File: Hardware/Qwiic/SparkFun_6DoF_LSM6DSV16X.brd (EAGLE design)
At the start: 25.4 x 25.4 mm, 70 parts, among them J1 QWIIC_RIGHT_ANGLE, J2 QWIIC_RIGHT_ANGLE, U2 LSM6DSV16X

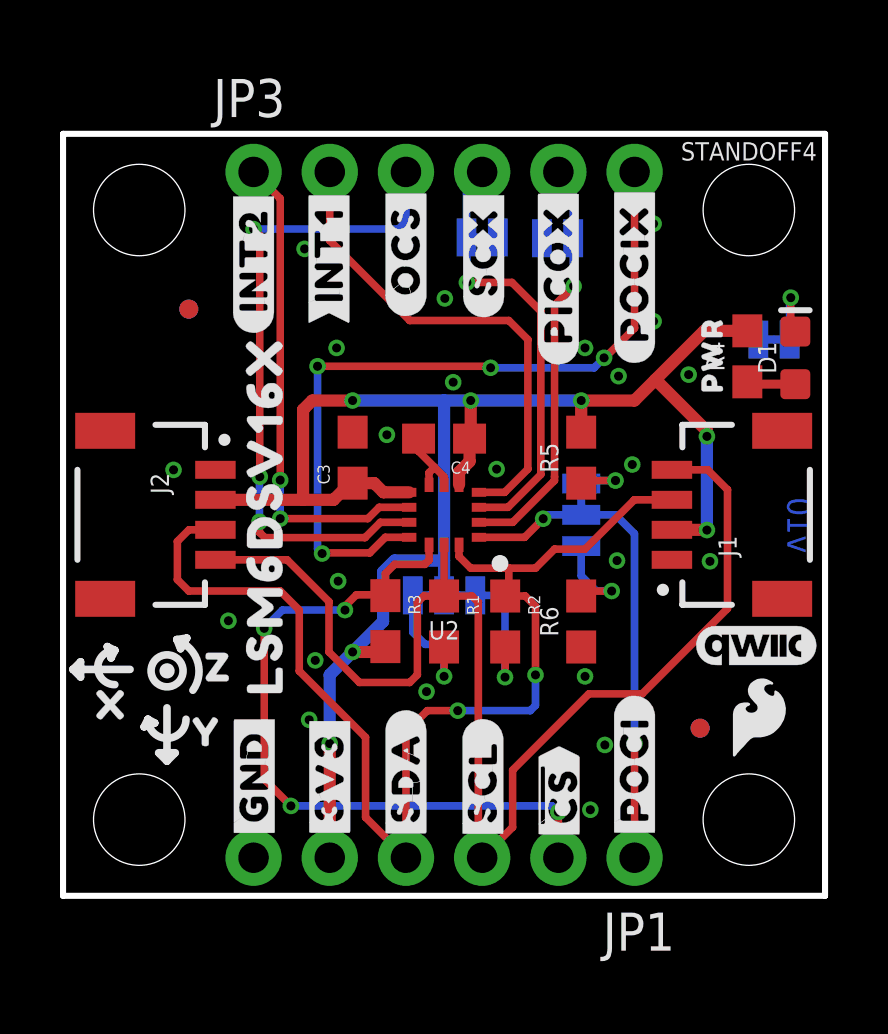
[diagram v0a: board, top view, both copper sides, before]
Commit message: Changes design to design with filter
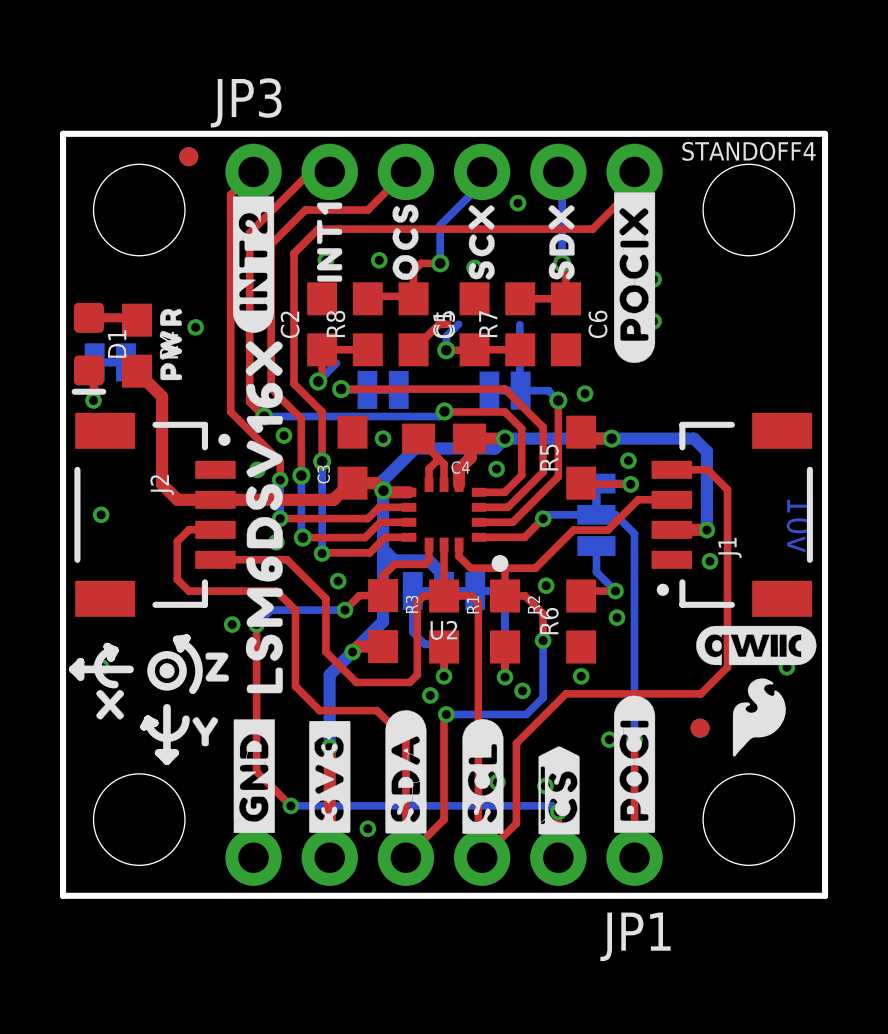
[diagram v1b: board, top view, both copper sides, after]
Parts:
- removed FRAME1: FRAME-LETTER, SparkFun-Aesthetics:CREATIVE_COMMONS
- removed U$19: (no value), bot:#INT1#9
- removed U$20: (no value), bot:#OCS#7
- removed U$21: (no value), top:LSM6DSV16X37
- added C1, C2, C5, C6: 110pF, SparkFun-Capacitors:0603
- added FRAME2: FRAME-LEDGER, SparkFun-Aesthetics:CREATIVE_COMMONS
- added R7, R8: 0, SparkFun-Resistors:0603
- added U$32: (no value), top:OCS17
- added U$41: (no value), top:INT16
- added U$42: (no value), top:#SDX#20
- added U$43: (no value), top:#SCX#19
- added U$44: (no value), top:#FILT1#21
- added U$45: (no value), top:#FILT2#21
- added U$46: (no value), top:LSM6DSV16X37
- U$10: device top:#SCX#9 -> top:SCX18
- U$11: device ISMTop:#PICOX#10 -> top:SDX19
- U$23: device bot:#SCX#8 -> top:SCX18
- U$30: device bot:#SDX#28 -> top:SDX19
- U$7: device top:#INT1#9 -> top:INT16
- U$9: device top:#OCS#8 -> top:OCS17
- moved D1 23.6 mm to (0.86, 18.4), turned to 270 degrees
- moved LED 22.1 mm to (1.57, 17.8), turned to 0 degrees
- moved U$16 22.1 mm to (1.65, 19.3)
- moved R4 20.3 mm to (2.46, 18.3), turned to 270 degrees
- moved U$28 18.0 mm to (3.61, 18.4)
- moved SCX 6.06 mm to (10.7, 16.9)
- moved SDX 5.37 mm to (14.7, 16.8)
- moved FD1 5.08 mm to (4.19, 24.6)
- moved FID1 5.08 mm to (4.19, 24.6)
- moved U$30 2.54 mm to (16.5, 21.6)
- moved U$23 2.52 mm to (13.8, 21.6)
- moved U$31 2.29 mm to (7.98, 12.7)
- moved U$11 1.12 mm to (16.6, 21.8)
- moved U$14 0.63 mm to (15.2, 13.3)
- moved U$13 0.57 mm to (15.1, 12.1)
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- renumbered U$12 to U$47
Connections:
- removed net SCX: JP3.4, SCX.2, U2.P3
- removed net SDX/PICO_AUX: JP3.5, SDX.2, U2.P2
- new net SCX/AH2/QVAR2: C5.1, JP3.4, R8.2
- new net SCX/AH2/QVAR2_FILTER: C2.1, R8.1, SCX.2, U2.P3
- new net SDX/AH1/QVAR1: C6.1, JP3.5, R7.2
- new net SDX/AH1/QVAR1_FILTER: C1.1, R7.1, SDX.2, U2.P2
- net GND: now also C1.2, C2.2, C5.2, C6.2
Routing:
- net SCX/AH2/QVAR2_FILTER: track 0.00 -> 15.8 mm, vias 0 -> 2
- net SCX: track 14.7 -> 0.00 mm, vias 1 -> 0
- net SDX/PICO_AUX: track 13.9 -> 0.00 mm, vias 1 -> 0
- net SDX/AH1/QVAR1_FILTER: track 0.00 -> 12.9 mm, vias 0 -> 2
- net SCX/AH2/QVAR2: track 0.00 -> 7.78 mm, vias 0 -> 1
- net SDX/AH1/QVAR1: track 0.00 -> 5.86 mm, vias 0 -> 1
- net 3.3V: track 56.8 -> 50.9 mm, vias 7 -> 6
- net INT1: track 16.5 -> 22.0 mm, vias 0 -> 2
- net OCS: track 22.3 -> 19.5 mm, vias 3 -> 2
- net GND: track 2.56 -> 4.38 mm, vias 23 -> 29
- net SCL: track 43.3 -> 44.9 mm
- net SDA/PICO: track 39.9 -> 40.6 mm
- net INT2: track 16.4 -> 17.0 mm
- net POCI_AUX: track 25.8 -> 26.3 mm, vias 4 -> 2
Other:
- board text added: "Elias Santistevan"
- board text added: "v01"
- board text removed: "v10"

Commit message: Adds labels, fixes various DRC issues
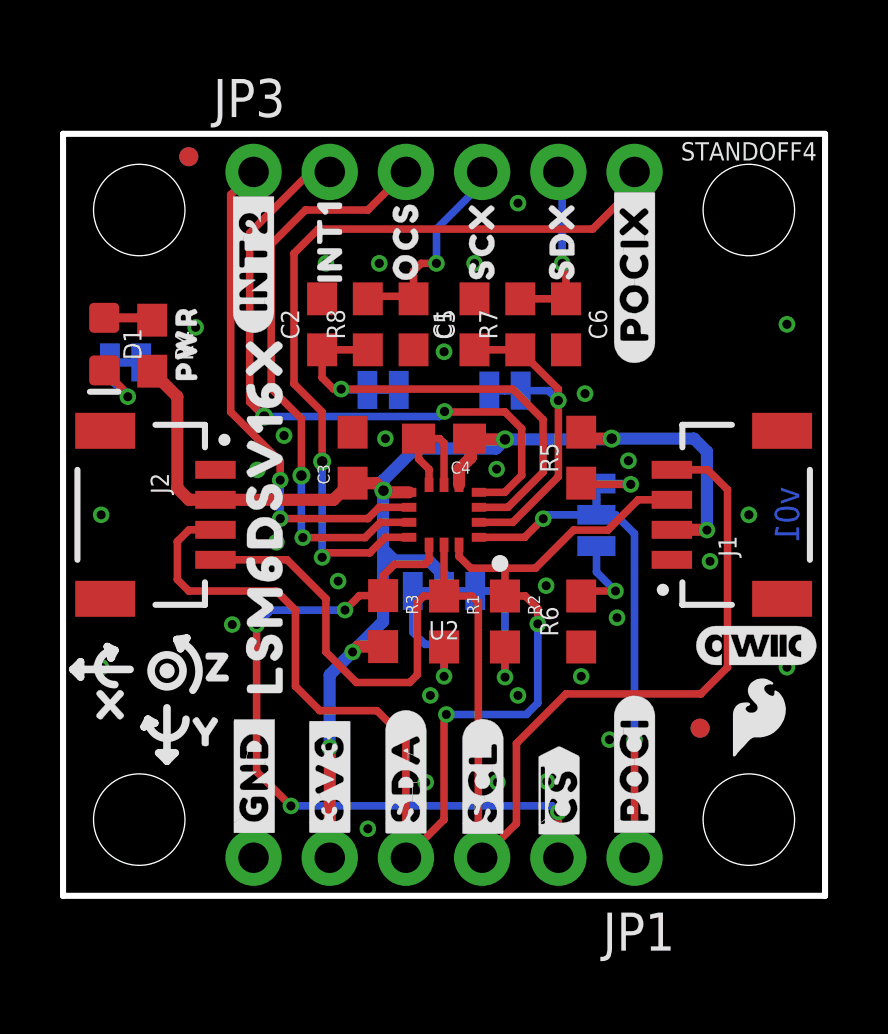
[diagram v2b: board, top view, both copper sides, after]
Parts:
- removed U$23: (no value), top:SCX18
- removed U$30: (no value), top:SDX19
- removed U$32: (no value), top:OCS17
- removed U$41: (no value), top:INT16
- removed U$44: (no value), top:#FILT1#21
- removed U$45: (no value), top:#FILT2#21
- added U$12: (no value), bot:#AH1#32
- added U$19: (no value), bot:#AH2#32
- added U$20: (no value), bot:#OCS#32
- added U$21: (no value), top:#INT1#25
- moved LED 0.51 mm to (2.08, 17.8)
- moved R4 0.51 mm to (2.97, 18.3)
- moved U$28 0.51 mm to (4.11, 18.4)
- moved D1 0.51 mm to (1.37, 18.4)
- moved U$16 0.51 mm to (2.16, 19.3)
- moved LOGO3 0.28 mm to (4.37, 12.7)
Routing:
- net SDX/AH1/QVAR1_FILTER: track 12.9 -> 11.0 mm, vias 2 -> 1
- net 3.3V: track 50.9 -> 50.0 mm
- net SCX/AH2/QVAR2: track 7.78 -> 7.23 mm
- net GND: track 4.38 -> 3.99 mm, vias 29 -> 31
- net SCX/AH2/QVAR2_FILTER: track 15.8 -> 15.7 mm, vias 2 -> 1

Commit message: Updates measures, fixes various DRC issues in micro
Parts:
- moved FRAME2 10.2 mm to (-17.8, -22.9)
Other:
- board text added: "Units in Inches"
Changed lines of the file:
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@@
 <layer number="45" name="Holes" color="7" fill="1" visible="yes" active="yes"/>
 <layer number="46" name="Milling" color="3" fill="1" visible="no" active="yes"/>
-<layer number="47" name="Measures" color="7" fill="1" visible="no" active="yes"/>
+<layer number="47" name="Measures" color="7" fill="1" visible="yes" active="yes"/>
 <layer number="48" name="Document" color="7" fill="1" visible="no" active="yes"/>
 <layer number="49" name="Reference" color="13" fill="1" visible="yes" active="yes"/>
@@
 <wire x1="22.5663125" y1="9.3805375" x2="23.2806875" y2="8.6661625" width="0.2032" layer="22"/>
 <wire x1="23.241" y1="9.3805375" x2="22.526625" y2="8.6661625" width="0.2032" layer="22"/>
-<dimension x1="0" y1="25.4" x2="0" y2="0" x3="-8.636" y3="12.7" textsize="1.778" textratio="15" layer="47" unit="inch" visible="yes"/>
-<dimension x1="25.4" y1="25.4" x2="0" y2="25.4" x3="12.7" y3="30.48" textsize="1.778" textratio="15" layer="47" unit="inch" visible="yes"/>
-<dimension x1="5.08" y1="12.7" x2="5.08" y2="0" x3="-5.588" y3="6.35" textsize="1.778" textratio="15" layer="47" unit="inch" visible="yes"/>
+<dimension x1="0" y1="25.4" x2="0" y2="0" x3="-8.636" y3="12.7" textsize="1.778" textratio="15" layer="47" unit="inch"/>
+<dimension x1="25.4" y1="25.4" x2="0" y2="25.4" x3="12.7" y3="30.48" textsize="1.778" textratio="15" layer="47" unit="inch"/>
+<dimension x1="5.08" y1="12.7" x2="5.08" y2="0" x3="-5.588" y3="6.35" textsize="1.778" textratio="15" layer="47" unit="inch"/>
 <dimension x1="2.54" y1="2.54" x2="2.54" y2="0" x3="-1.778" y3="1.27" textsize="1.778" textratio="15" layer="47" unit="inch"/>
-<dimension x1="2.54" y1="22.86" x2="2.54" y2="25.4" x3="-2.54" y3="24.13" textsize="1.778" textratio="15" layer="47" unit="inch" visible="yes"/>
-<dimension x1="2.54" y1="22.86" x2="22.86" y2="22.86" x3="12.7" y3="27.178" textsize="1.778" textratio="15" layer="47" unit="inch" visible="yes"/>
+<dimension x1="2.54" y1="22.86" x2="2.54" y2="25.4" x3="-2.54" y3="24.13" textsize="1.778" textratio="15" layer="47" unit="inch"/>
+<dimension x1="2.54" y1="22.86" x2="22.86" y2="22.86" x3="12.7" y3="27.178" textsize="1.778" textratio="15" layer="47" unit="inch"/>
 <rectangle x1="12.446" y1="13.462" x2="12.4968" y2="13.7668" layer="41"/>
-<text x="12.7" y="-12.7" size="1.778" layer="51" font="vector">Elias Santistevan</text>
+<text x="12.7" y="-22.86" size="1.778" layer="51" font="vector">Elias Santistevan</text>
+<text x="-26.67" y="-3.81" size="1.778" layer="47" font="vector">Units in Inches</text>
+<dimension x1="6.35" y1="1.27" x2="0" y2="1.27" x3="3.175" y3="-7.62" textsize="1.778" layer="47" unit="inch"/>
+<dimension x1="0" y1="0" x2="19.05" y2="0" x3="9.525" y3="-12.7" textsize="1.778" layer="47" unit="inch"/>
 </plain>
 <attributes>
@@
 <attribute name="VALUE" value="0" x="10.922" y="19.05" size="0.6096" layer="27" font="vector" ratio="20" rot="R90" align="top-center"/>
 </element>
-<element name="FRAME2" library="SparkFun-Aesthetics" package="CREATIVE_COMMONS" value="FRAME-LEDGER" x="-17.78" y="-12.7" smashed="yes">
-<attribute name="DESIGNER" value="" x="-17.78" y="-12.7" size="1.778" layer="27" display="off"/>
-<attribute name="REV" value="" x="-17.78" y="-12.7" size="1.778" layer="27" display="off"/>
+<element name="FRAME2" library="SparkFun-Aesthetics" package="CREATIVE_COMMONS" value="FRAME-LEDGER" x="-17.78" y="-22.86" smashed="yes">
+<attribute name="DESIGNER" value="" x="-17.78" y="-22.86" size="1.778" layer="27" display="off"/>
+<attribute name="REV" value="" x="-17.78" y="-22.86" size="1.778" layer="27" display="off"/>
 </element>
 <element name="U$7" library="top" package="INT16" value="" x="8.89" y="21.844" smashed="yes" rot="R90"/>

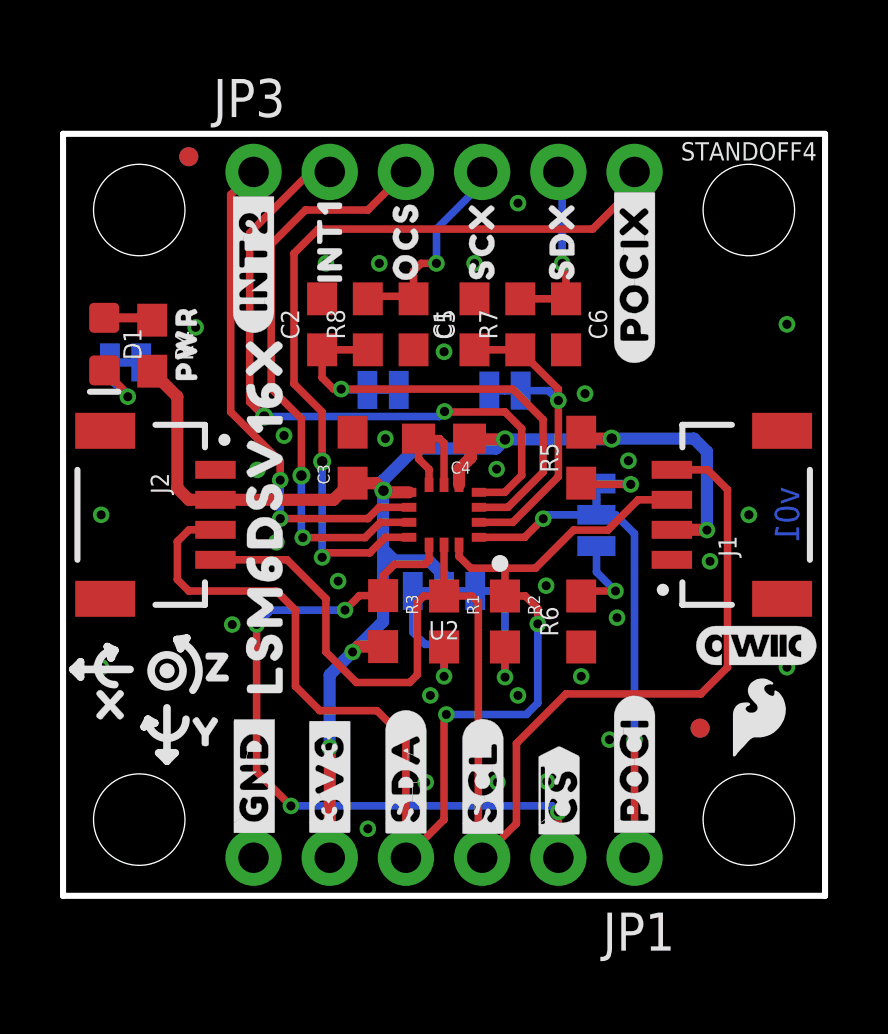
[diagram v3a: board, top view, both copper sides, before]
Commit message: Updates part with silk outline
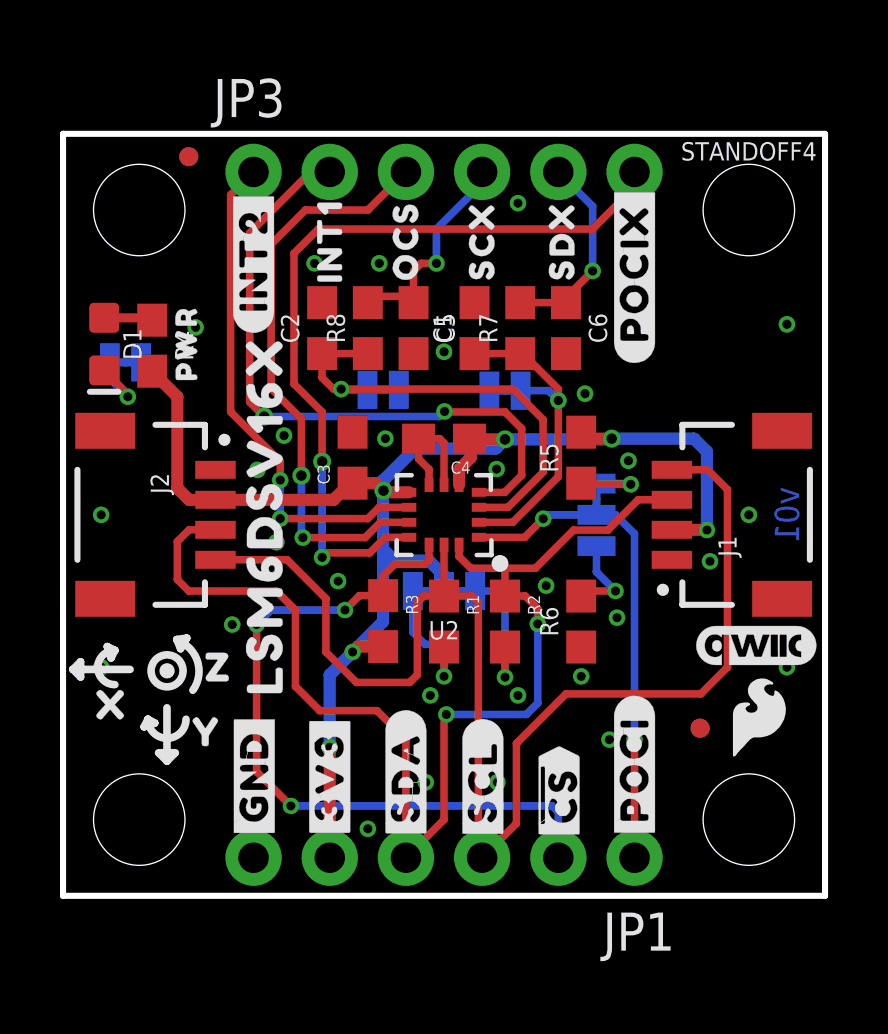
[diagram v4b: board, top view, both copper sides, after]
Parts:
- moved U$13 0.25 mm to (15.1, 11.9)
- moved U$14 0.25 mm to (15.2, 13.5)
- moved C1 0.13 mm to (13.7, 18.9)
- moved C2 0.13 mm to (8.64, 18.9)
- moved C5 0.13 mm to (11.7, 18.9)
- moved C6 0.13 mm to (16.8, 18.9)
- moved R7 0.13 mm to (15.2, 18.9)
- moved R8 0.13 mm to (10.2, 18.9)
- moved U$43 0.13 mm to (10.7, 15.4)
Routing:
- net SDX/AH1/QVAR1: track 5.86 -> 6.72 mm
- net SCX/AH2/QVAR2: track 7.23 -> 7.85 mm
- net GND: vias 31 -> 29
- net !CS!: vias 4 -> 3
